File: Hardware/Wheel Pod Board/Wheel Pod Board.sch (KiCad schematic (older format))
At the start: 24 parts, among them U1 STM32F401RCT6

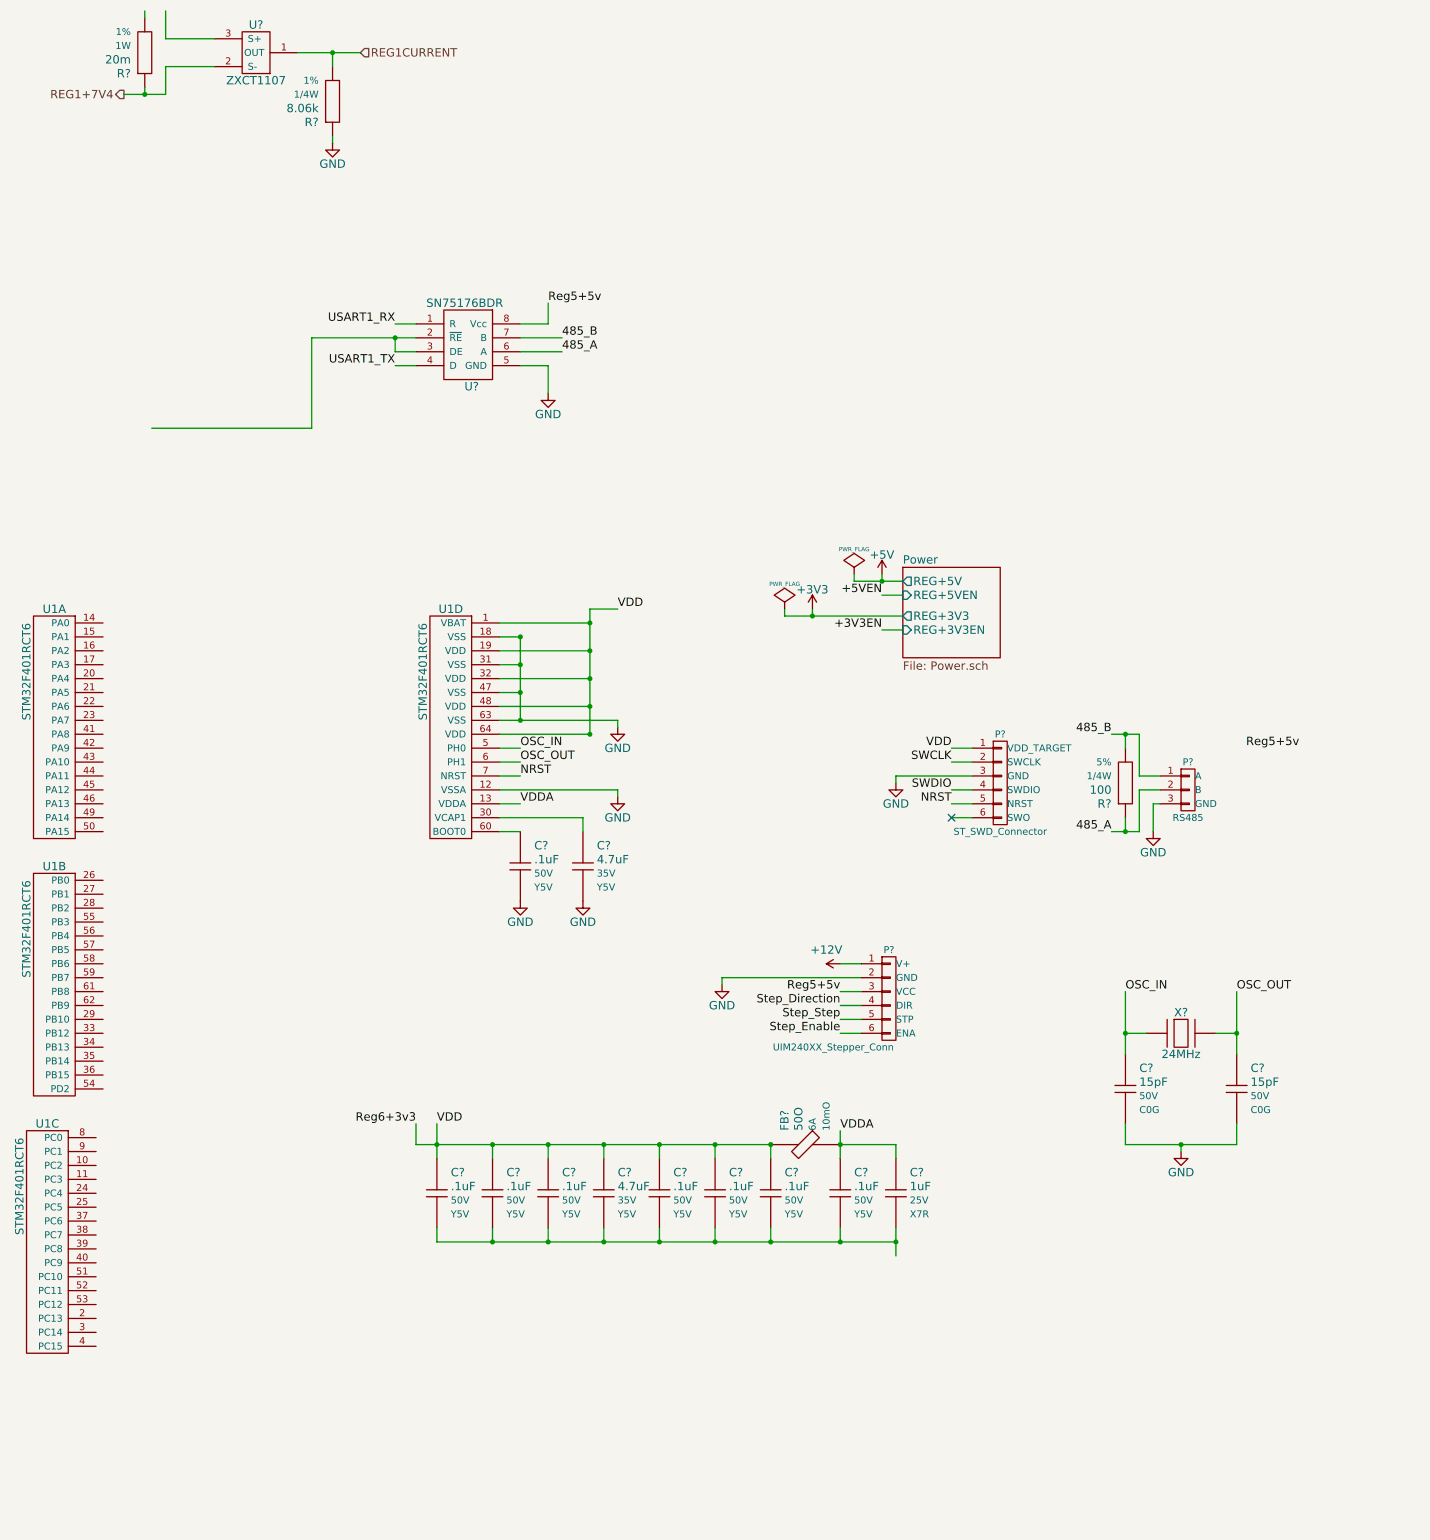
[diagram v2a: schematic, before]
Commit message: Connect current sense, more connectors
Resistor values not correct #6
Resolve #2
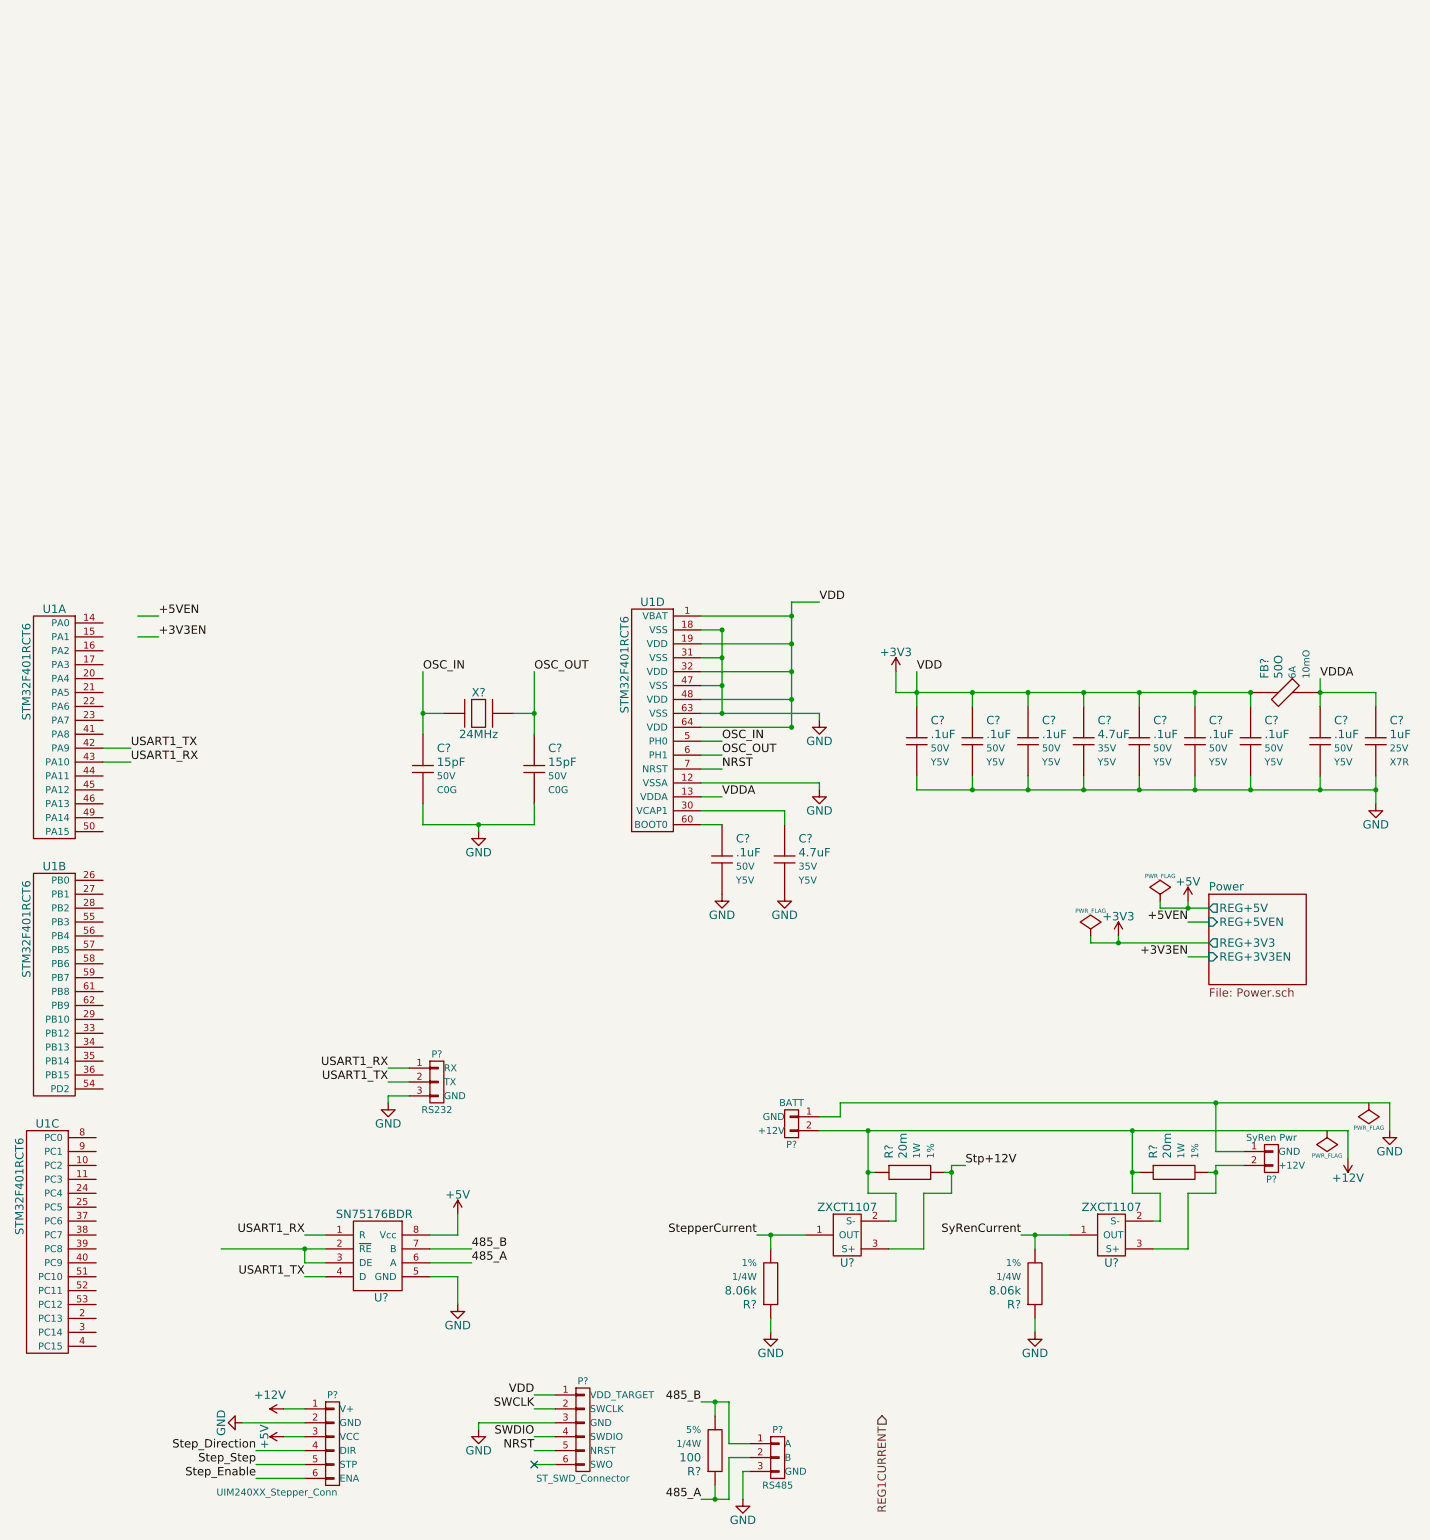
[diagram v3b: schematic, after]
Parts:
- added P?: BATT, symbol BATT
- added P?: SyRen Pwr, symbol BATT
- added P?: RS232, symbol RS232
- added R?: 20m, Resistors_SMD:R_1206_HandSoldering, symbol Resistor
- added R?: 8.06k, Resistors_SMD:R_1206_HandSoldering, symbol Resistor
- added U?: ZXCT1107, Housings_SOT-23_SOT-143_TSOT-6:SOT23_Transistor_Handsoldering_RevB_14Mar2014, symbol ZXCT1107
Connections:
- net labels added: StepperCurrent, Stp+12V, SyRenCurrent
- net labels removed: REG1+7V4, Reg5+5v, Reg6+3v3
- wire segments 140 -> 138
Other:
- moved on the sheet: C?, FB?, P?, R?, U1D, U?, X?

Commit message: Delete some random labels
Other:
- moved on the sheet: P?
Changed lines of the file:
@@
 	1    0    0    -1
 $EndComp
-Text HLabel 7250 6850 3    60   Input ~ 0
-REG1CURRENT
 Wire Wire Line
 	7550 5250 7550 5650
@@
 L RS232 P?
 U 1 1 54FB0485
-P 4050 4450
-F 0 "P?" H 4050 4650 50  0000 C CNN
-F 1 "RS232" H 4050 4250 50  0000 C CNN
-F 2 "" H 4050 4450 60  0000 C CNN
-F 3 "" H 4050 4450 60  0000 C CNN
-	1    4050 4450
-	1    0    0    -1
-$EndComp
-Wire Wire Line
-	3850 4550 3700 4550
-Wire Wire Line
-	3700 4550 3700 4600
+P 3700 4650
+F 0 "P?" H 3700 4850 50  0000 C CNN
+F 1 "RS232" H 3700 4450 50  0000 C CNN
+F 2 "" H 3700 4650 60  0000 C CNN
+F 3 "" H 3700 4650 60  0000 C CNN
+	1    3700 4650
+	1    0    0    -1
+$EndComp
+Wire Wire Line
+	3500 4750 3350 4750
+Wire Wire Line
+	3350 4750 3350 4800
 $Comp
 L GND #PWR?
 U 1 1 54FB0646
-P 3700 4600
-F 0 "#PWR?" H 3700 4350 60  0001 C CNN
-F 1 "GND" H 3700 4450 60  0000 C CNN
-F 2 "" H 3700 4600 60  0000 C CNN
-F 3 "" H 3700 4600 60  0000 C CNN
-	1    3700 4600
-	1    0    0    -1
-$EndComp
-Text Label 3700 4350 2    60   ~ 0
+P 3350 4800
+F 0 "#PWR?" H 3350 4550 60  0001 C CNN
+F 1 "GND" H 3350 4650 60  0000 C CNN
+F 2 "" H 3350 4800 60  0000 C CNN
+F 3 "" H 3350 4800 60  0000 C CNN
+	1    3350 4800
+	1    0    0    -1
+$EndComp
+Text Label 3350 4550 2    60   ~ 0
 USART1_RX
-Text Label 3700 4450 2    60   ~ 0
+Text Label 3350 4650 2    60   ~ 0
 USART1_TX
 Wire Wire Line
-	3700 4450 3850 4450
-Wire Wire Line
-	3700 4350 3850 4350
+	3350 4650 3500 4650
+Wire Wire Line
+	3350 4550 3500 4550
 $EndSCHEMATC
